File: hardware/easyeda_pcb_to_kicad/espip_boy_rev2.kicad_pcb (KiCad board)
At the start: 4 copper layers, 35 x 45 mm, 111 parts, among them CN1 1X4, P2 CONN_01X04, Q1 SS8050/Y1, Q2 SS8050/Y1, Q3 DMG1012T-7, Q4 DMG1012T-7, Q5 SS8050/Y1, SW1 TS24CA 250GF 013, SW4 TS24CA 250GF 013, U1 LTR-390UV-01, U10 ICS-43434_C5656610, U11 ME6217A33PG, U12 BQ24074RGTR, U13 MAX30102EFD+T_C6454833, U14 BQ27421YZFR-G1A, U15 200_mah_lipo, U17 MAX98357AETE+T, U18 ME6206B18XG, U2 CP2102N-A02-GQFN28R, U3 0402 Blue, U4 GT-USB-7010ASV, U5 BMI270, U7 YSN8010SJ 32.768KHZ, U8 ESP32-WROOM-32E(8MB), U9 LIS2MDLTR

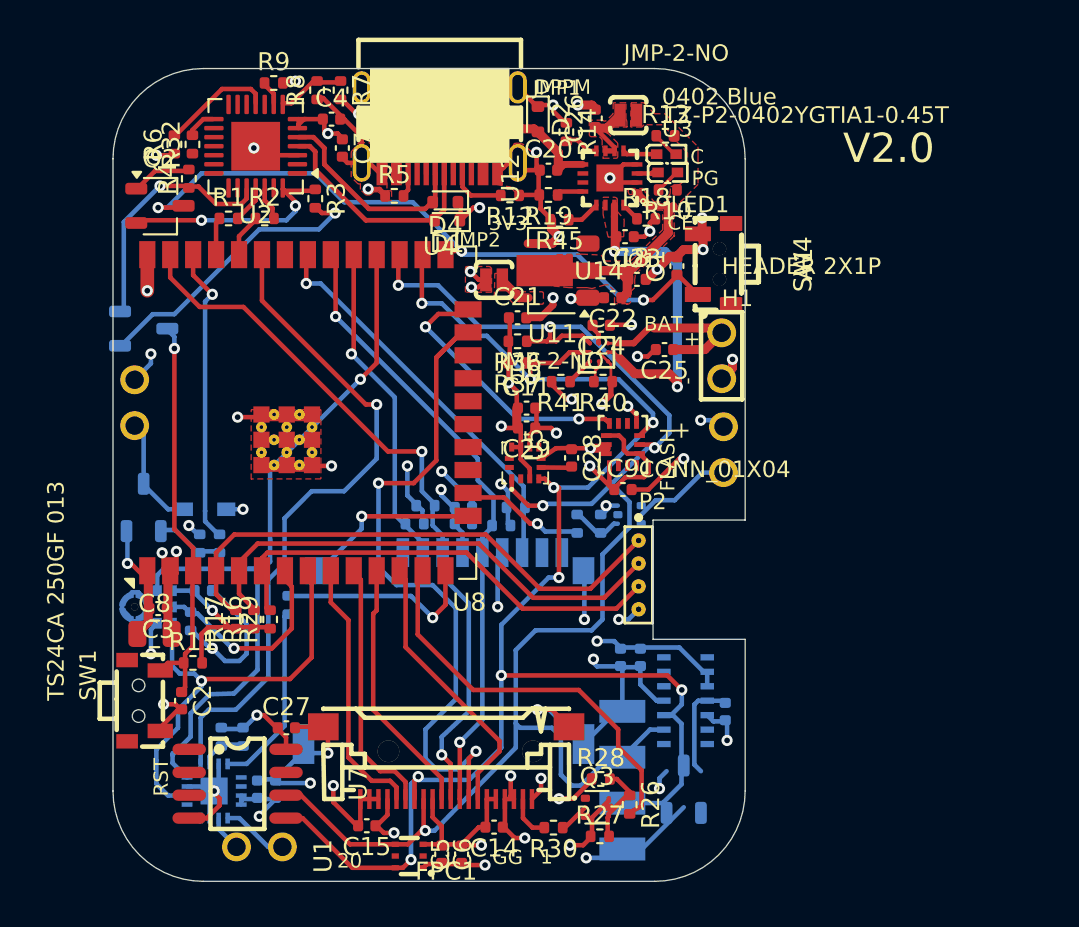
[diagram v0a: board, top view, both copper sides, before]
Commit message: Completed assembly of Rev 2 pcb, battery, display and digital crown
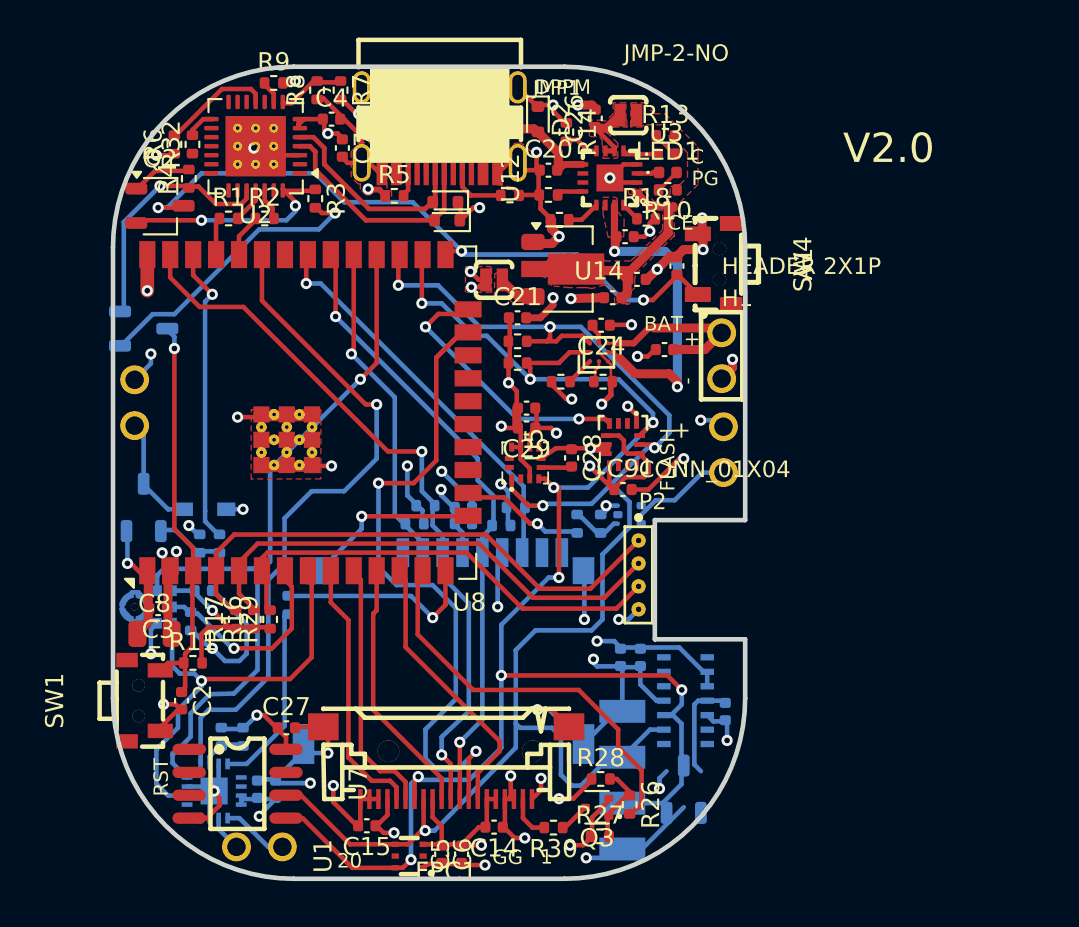
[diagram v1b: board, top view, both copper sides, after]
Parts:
- LED1: footprint espip_boy_rev2:LED0402-RD_GREEN -> LED_SMD:LED_0402_1005Metric
- SW1: footprint espip_boy_rev2:SW-SMD_L4.7-W3.5-P3.35-EH -> easyeda2kicad:SW-SMD_L4.7-W3.5-P3.35-EH
- U2: footprint Package_DFN_QFN:QFN-28-1EP_5x5mm_P0.5mm_EP2.7x2.7mm -> Package_DFN_QFN:QFN-28-1EP_5x5mm_P0.5mm_EP3.35x3.35mm_ThermalVias
- U3: footprint espip_boy_rev2:LED0402-RD -> LED_SMD:LED_0402_1005Metric
- moved U11 0.87 mm to (160.5, 95.6), turned to 0 degrees
- turned Q3 to 180 degrees
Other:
- outline, holes or cut-outs redrawn
- board text removed: "IO1"
